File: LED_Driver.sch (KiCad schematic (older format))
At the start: 0 parts

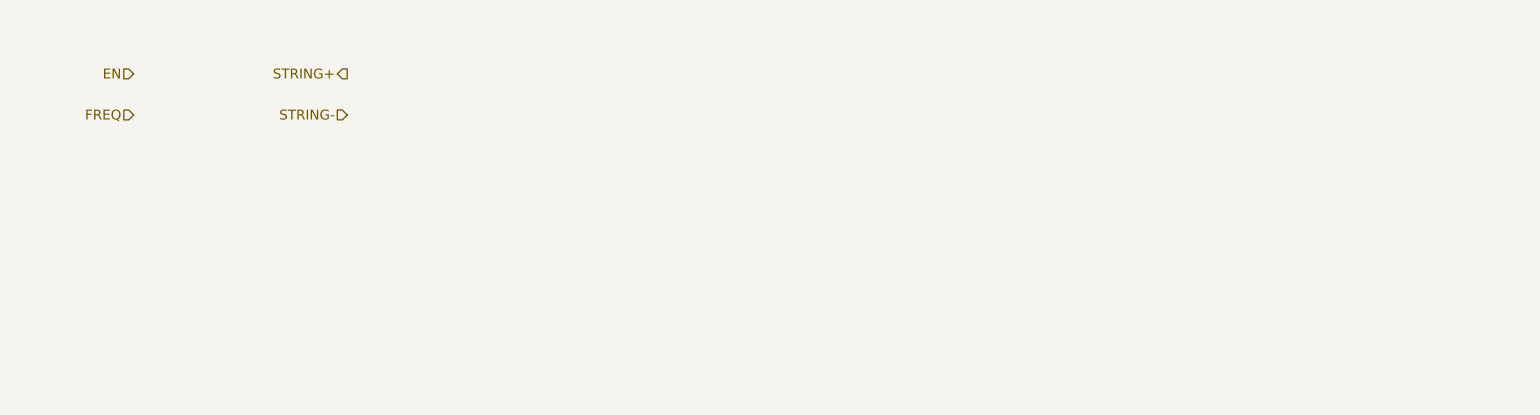
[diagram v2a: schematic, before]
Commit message: Blocked out the LED Driver and Power sheets
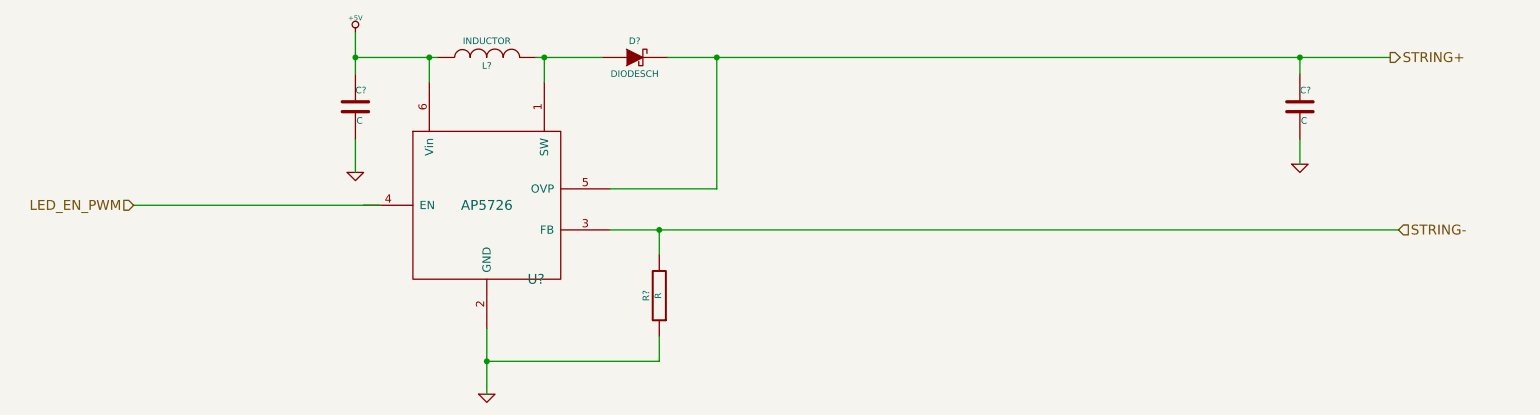
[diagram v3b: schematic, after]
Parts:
- added C? (x2): C, ~, symbol C
- added D?: DIODESCH, ~, symbol DIODESCH
- added L?: INDUCTOR, ~, symbol INDUCTOR
- added R?: R, ~, symbol R
- added U?: AP5726, symbol AP5726
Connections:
- net labels added: +5V, GND, LED_EN_PWM
- net labels removed: EN, FREQ
- wire segments 0 -> 17
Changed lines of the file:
@@
 LIBS:contrib
 LIBS:valves
+LIBS:CE_BenchBuddEE-cache
 LIBS:CE_BenchBuddEE
 LIBS:CE_BenchBuddEE-cache
@@
 $Descr A4 11693 8268
 encoding utf-8
-Sheet 3 8
+Sheet 8 9
 Title ""
-Date "5 feb 2014"
+Date "6 feb 2014"
 Rev ""
 Comp ""
@@
 Comment4 ""
 $EndDescr
-Text HLabel 2500 2600 0    60   Input ~ 0
-EN
-Text HLabel 2500 2850 0    60   Input ~ 0
-FREQ
-Text HLabel 3800 2600 0    60   Output ~ 0
+Text HLabel 2500 3400 0    60   Input ~ 0
+LED_EN_PWM
+Text HLabel 10150 2500 2    60   Output ~ 0
 STRING+
-Text HLabel 3800 2850 0    60   Input ~ 0
+Text HLabel 10200 3550 2    60   Input ~ 0
 STRING-
+$Comp
+L AP5726 U?
+U 1 1 52F311DA
+P 4650 3400
+F 0 "U?" H 4950 2950 60  0000 C CNN
+F 1 "AP5726" H 4650 3400 60  0000 C CNN
+F 2 "" H 4650 3400 60  0000 C CNN
+F 3 "" H 4650 3400 60  0000 C CNN
+	1    4650 3400
+	1    0    0    -1
+$EndComp
+Wire Wire Line
+	4000 3400 2500 3400
+$Comp
+L INDUCTOR L?
+U 1 1 52F311ED
+P 4650 2500
+F 0 "L?" V 4600 2500 40  0000 C CNN
+F 1 "INDUCTOR" V 4750 2500 40  0000 C CNN
+F 2 "~" H 4650 2500 60  0000 C CNN
+F 3 "~" H 4650 2500 60  0000 C CNN
+	1    4650 2500
+	0    -1   -1   0
+$EndComp
+Wire Wire Line
+	4300 2650 4300 2500
+Wire Wire Line
+	3850 2500 4350 2500
+Wire Wire Line
+	5000 2650 5000 2500
+Wire Wire Line
+	4950 2500 5350 2500
+$Comp
+L +5V #PWR?
+U 1 1 52F312CC
+P 3850 2350
+F 0 "#PWR?" H 3850 2440 20  0001 C CNN
+F 1 "+5V" H 3850 2440 30  0000 C CNN
+F 2 "~" H 3850 2350 60  0000 C CNN
+F 3 "~" H 3850 2350 60  0000 C CNN
+	1    3850 2350
+	1    0    0    -1
+$EndComp
+$Comp
+L C C?
+U 1 1 52F312DB
+P 3850 2800
+F 0 "C?" H 3850 2900 40  0000 L CNN
+F 1 "C" H 3856 2715 40  0000 L CNN
+F 2 "~" H 3888 2650 30  0000 C CNN
+F 3 "~" H 3850 2800 60  0000 C CNN
+	1    3850 2800
+	1    0    0    -1
+$EndComp
+Wire Wire Line
+	3850 2350 3850 2600
+Connection ~ 4300 2500
+Connection ~ 3850 2500
+$Comp
+L GND #PWR?
+U 1 1 52F312F8
+P 3850 3200
+F 0 "#PWR?" H 3850 3200 30  0001 C CNN
+F 1 "GND" H 3850 3130 30  0001 C CNN
+F 2 "~" H 3850 3200 60  0000 C CNN
+F 3 "~" H 3850 3200 60  0000 C CNN
+	1    3850 3200
+	1    0    0    -1
+$EndComp
+Wire Wire Line
+	3850 3000 3850 3200
+$Comp
+L DIODESCH D?
+U 1 1 52F3136A
+P 5550 2500
+F 0 "D?" H 5550 2600 40  0000 C CNN
+F 1 "DIODESCH" H 5550 2400 40  0000 C CNN
+F 2 "~" H 5550 2500 60  0000 C CNN
+F 3 "~" H 5550 2500 60  0000 C CNN
+	1    5550 2500
+	1    0    0    -1
+$EndComp
+Connection ~ 5000 2500
+Wire Wire Line
+	5400 3300 6050 3300
+Wire Wire Line
+	6050 3300 6050 2500
+Wire Wire Line
+	5750 2500 10150 2500
+$Comp
+L C C?
+U 1 1 52F31397
+P 9600 2800
+F 0 "C?" H 9600 2900 40  0000 L CNN
+F 1 "C" H 9606 2715 40  0000 L CNN
+F 2 "~" H 9638 2650 30  0000 C CNN
+F 3 "~" H 9600 2800 60  0000 C CNN
+	1    9600 2800
+	1    0    0    -1
+$EndComp
+Wire Wire Line
+	9600 2500 9600 2600
+Connection ~ 6050 2500
+Connection ~ 9600 2500
+$Comp
+L R R?
+U 1 1 52F313C5
+P 5700 3950
+F 0 "R?" V 5780 3950 40  0000 C CNN
+F 1 "R" V 5707 3951 40  0000 C CNN
+F 2 "~" V 5630 3950 30  0000 C CNN
+F 3 "~" H 5700 3950 30  0000 C CNN
+	1    5700 3950
+	-1   0    0    1
+$EndComp
+$Comp
+L GND #PWR?
+U 1 1 52F313D4
+P 4650 4550
+F 0 "#PWR?" H 4650 4550 30  0001 C CNN
+F 1 "GND" H 4650 4480 30  0001 C CNN
+F 2 "~" H 4650 4550 60  0000 C CNN
+F 3 "~" H 4650 4550 60  0000 C CNN
+	1    4650 4550
+	1    0    0    -1
+$EndComp
+Wire Wire Line
+	4650 4150 4650 4550
+Wire Wire Line
+	5400 3550 10200 3550
+Wire Wire Line
+	5700 4200 5700 4350
+Wire Wire Line
+	5700 3550 5700 3700
+Wire Wire Line
+	5700 4350 4650 4350
+Connection ~ 4650 4350
+Connection ~ 5700 3550
+$Comp
+L GND #PWR?
+U 1 1 52F314BD
+P 9600 3150
+F 0 "#PWR?" H 9600 3150 30  0001 C CNN
+F 1 "GND" H 9600 3080 30  0001 C CNN
+F 2 "~" H 9600 3150 60  0000 C CNN
+F 3 "~" H 9600 3150 60  0000 C CNN
+	1    9600 3150
+	1    0    0    -1
+$EndComp
+Wire Wire Line
+	9600 3000 9600 3150
 $EndSCHEMATC

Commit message: Completed Arduino Block Diagram and Fan Redesign
The commits as of this are now up to date with the videos released for
Contextual Electronics, Week 3.
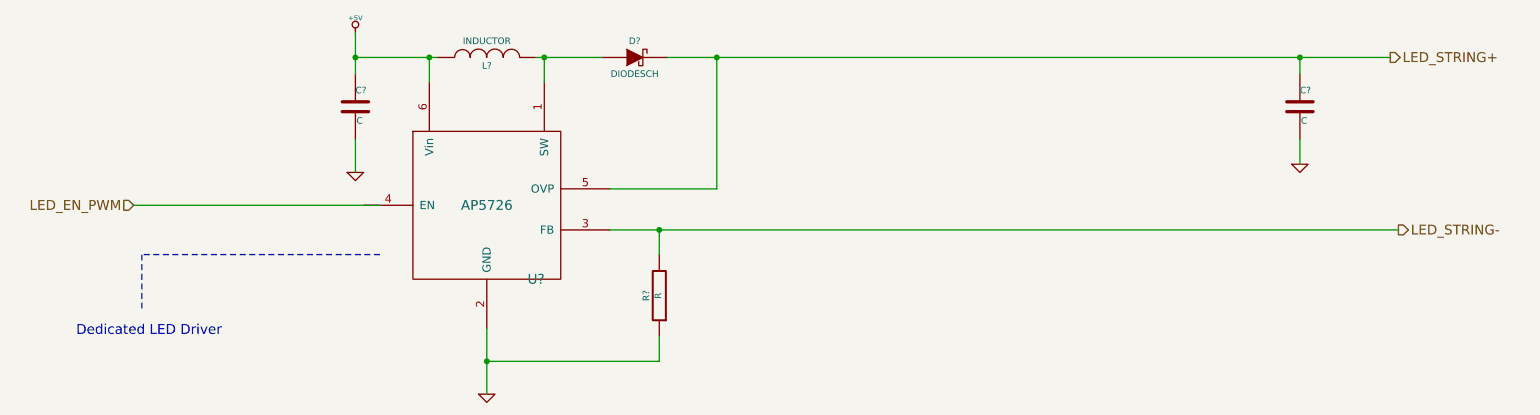
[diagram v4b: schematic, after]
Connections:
- net labels added: LED_STRING+, LED_STRING-
- net labels removed: STRING+, STRING-
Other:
- note added: "Dedicated LED Driver"
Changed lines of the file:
@@
 $Descr A4 11693 8268
 encoding utf-8
-Sheet 8 9
+Sheet 5 9
 Title ""
 Date "6 feb 2014"
@@
 LED_EN_PWM
 Text HLabel 10150 2500 2    60   Output ~ 0
-STRING+
-Text HLabel 10200 3550 2    60   Input ~ 0
-STRING-
+LED_STRING+
+Text HLabel 10200 3550 2    60   Output ~ 0
+LED_STRING-
 $Comp
 L AP5726 U?
@@
 Wire Wire Line
 	9600 3000 9600 3150
+Wire Notes Line
+	4000 3700 2550 3700
+Wire Notes Line
+	2550 3700 2550 4050
+Text Notes 2150 4200 0    60   ~ 0
+Dedicated LED Driver
 $EndSCHEMATC

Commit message: Initial layout of relay and thermocouple
All block diagrams completed through Week 3.  Component selection
spreadsheets created: Bench Buddy Session 1CE.xlsx = official part
selection and bom.xlsx is the version I came up with.

Part association and initial layout of the Relay and Thermocouple
sections completed.
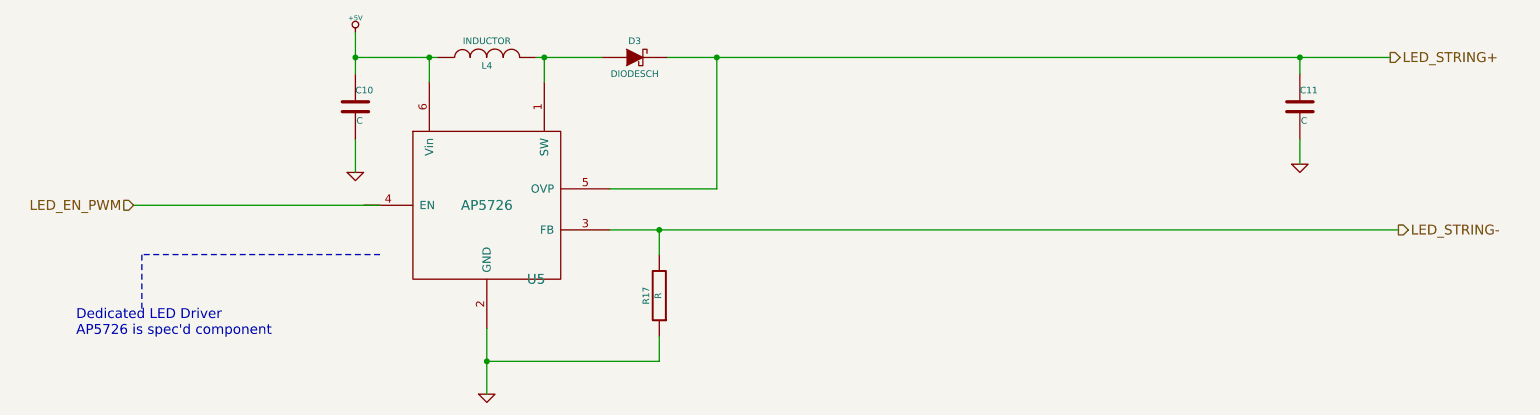
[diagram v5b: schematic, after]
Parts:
- gave numbers to parts that had none: 6
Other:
- note added: "Dedicated LED Driver\nAP5726 is spec'd component"
- note removed: "Dedicated LED Driver"
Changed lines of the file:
@@
 Sheet 5 9
 Title ""
-Date "6 feb 2014"
+Date "21 feb 2014"
 Rev ""
 Comp ""
@@
 LED_STRING-
 $Comp
-L AP5726 U?
+L AP5726 U5
 U 1 1 52F311DA
 P 4650 3400
-F 0 "U?" H 4950 2950 60  0000 C CNN
+F 0 "U5" H 4950 2950 60  0000 C CNN
 F 1 "AP5726" H 4650 3400 60  0000 C CNN
 F 2 "" H 4650 3400 60  0000 C CNN
@@
 	4000 3400 2500 3400
 $Comp
-L INDUCTOR L?
+L INDUCTOR L4
 U 1 1 52F311ED
 P 4650 2500
-F 0 "L?" V 4600 2500 40  0000 C CNN
+F 0 "L4" V 4600 2500 40  0000 C CNN
 F 1 "INDUCTOR" V 4750 2500 40  0000 C CNN
 F 2 "~" H 4650 2500 60  0000 C CNN
@@
 	4950 2500 5350 2500
 $Comp
-L +5V #PWR?
+L +5V #PWR034
 U 1 1 52F312CC
 P 3850 2350
-F 0 "#PWR?" H 3850 2440 20  0001 C CNN
+F 0 "#PWR034" H 3850 2440 20  0001 C CNN
 F 1 "+5V" H 3850 2440 30  0000 C CNN
 F 2 "~" H 3850 2350 60  0000 C CNN
@@
 $EndComp
 $Comp
-L C C?
+L C C10
 U 1 1 52F312DB
 P 3850 2800
-F 0 "C?" H 3850 2900 40  0000 L CNN
+F 0 "C10" H 3850 2900 40  0000 L CNN
 F 1 "C" H 3856 2715 40  0000 L CNN
 F 2 "~" H 3888 2650 30  0000 C CNN
@@
 Connection ~ 3850 2500
 $Comp
-L GND #PWR?
+L GND #PWR035
 U 1 1 52F312F8
 P 3850 3200
-F 0 "#PWR?" H 3850 3200 30  0001 C CNN
+F 0 "#PWR035" H 3850 3200 30  0001 C CNN
 F 1 "GND" H 3850 3130 30  0001 C CNN
 F 2 "~" H 3850 3200 60  0000 C CNN
@@
 	3850 3000 3850 3200
 $Comp
-L DIODESCH D?
+L DIODESCH D3
 U 1 1 52F3136A
 P 5550 2500
-F 0 "D?" H 5550 2600 40  0000 C CNN
+F 0 "D3" H 5550 2600 40  0000 C CNN
 F 1 "DIODESCH" H 5550 2400 40  0000 C CNN
 F 2 "~" H 5550 2500 60  0000 C CNN
@@
 	5750 2500 10150 2500
 $Comp
-L C C?
+L C C11
 U 1 1 52F31397
 P 9600 2800
-F 0 "C?" H 9600 2900 40  0000 L CNN
+F 0 "C11" H 9600 2900 40  0000 L CNN
 F 1 "C" H 9606 2715 40  0000 L CNN
 F 2 "~" H 9638 2650 30  0000 C CNN
@@
 Connection ~ 9600 2500
 $Comp
-L R R?
+L R R17
 U 1 1 52F313C5
 P 5700 3950
-F 0 "R?" V 5780 3950 40  0000 C CNN
+F 0 "R17" V 5780 3950 40  0000 C CNN
 F 1 "R" V 5707 3951 40  0000 C CNN
 F 2 "~" V 5630 3950 30  0000 C CNN
@@
 $EndComp
 $Comp
-L GND #PWR?
+L GND #PWR036
 U 1 1 52F313D4
 P 4650 4550
-F 0 "#PWR?" H 4650 4550 30  0001 C CNN
+F 0 "#PWR036" H 4650 4550 30  0001 C CNN
 F 1 "GND" H 4650 4480 30  0001 C CNN
 F 2 "~" H 4650 4550 60  0000 C CNN
@@
 Connection ~ 5700 3550
 $Comp
-L GND #PWR?
+L GND #PWR037
 U 1 1 52F314BD
 P 9600 3150
-F 0 "#PWR?" H 9600 3150 30  0001 C CNN
+F 0 "#PWR037" H 9600 3150 30  0001 C CNN
 F 1 "GND" H 9600 3080 30  0001 C CNN
 F 2 "~" H 9600 3150 60  0000 C CNN
@@
 	2550 3700 2550 4050
 Text Notes 2150 4200 0    60   ~ 0
-Dedicated LED Driver
+Dedicated LED Driver\nAP5726 is spec'd component
 $EndSCHEMATC

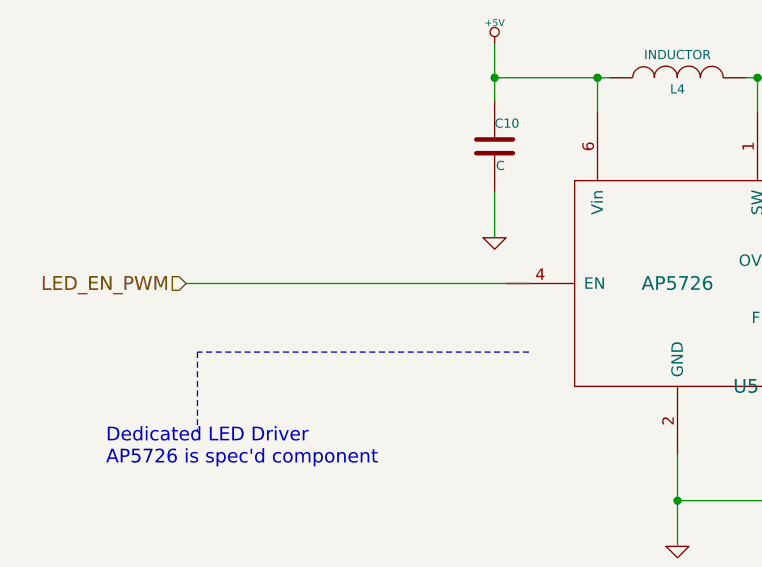
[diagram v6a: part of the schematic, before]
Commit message: Reorganization of power conditioning module
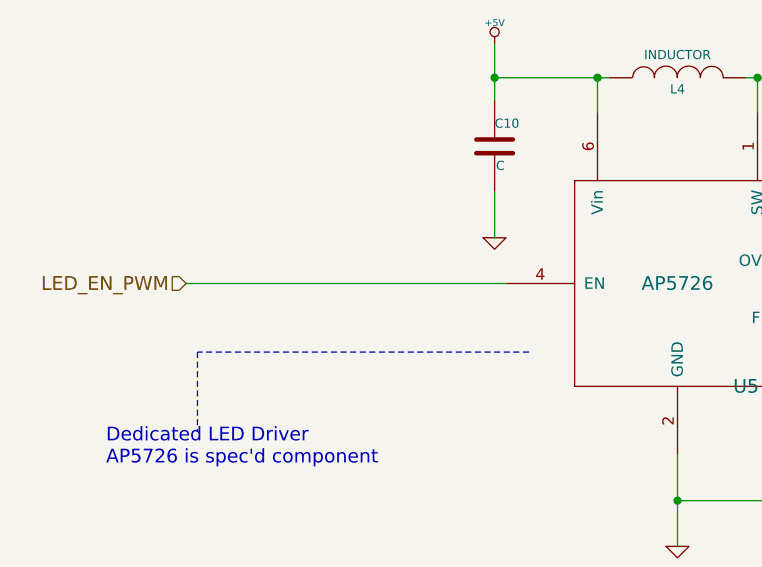
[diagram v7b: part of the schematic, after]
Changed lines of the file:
@@
 	1    0    0    -1
 $EndComp
-Wire Wire Line
-	4000 3400 2500 3400
 $Comp
 L INDUCTOR L4
@@
 Text Notes 2150 4200 0    60   ~ 0
 Dedicated LED Driver\nAP5726 is spec'd component
+Wire Wire Line
+	3900 3400 2500 3400
 $EndSCHEMATC
